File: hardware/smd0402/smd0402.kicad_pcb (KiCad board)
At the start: 2 copper layers, 140 x 40 mm, 79 parts, among them J1 Conn_01x04, J2 Conn_01x03, T1 TestPoint_THTPad_3.0x3.0mm_Dr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, T12 TestPoint_THTPad_3.0x3.0mm_Dr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, T13 TestPoint_THTPad_3.0x3.0mm_Dr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, T14 TestPoint_THTPad_3.0x3.0mm_Dr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, T15 TestPoint_THTPad_3.0x3.0mm_Dr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, T16 TestPoint_THTPad_3.0x3.0mm_Dr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, T18 TestPoint_THTPad_3.0x3.0mm_Dr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, T19 TestPoint_THTPad_3.0x3.0mm_Dr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, T20 TestPoint_THTPad_3.0x3.0mm_Dr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, T21 TestPoint_THTPad_3.0x3.0mm_Dr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, T22 TestPoint_THTPad_3.0x3.0mm_Dr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, T42 TestPoint_THTPad_D1.0mm_Drill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, T43 TestPoint_THTPad_D1.0mm_Drill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, T44 TestPoint_THTPad_D1.0mm_Drill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, T45 TestPoint_THTPad_D1.0mm_Drill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, T46 TestPoint_THTPad_D1.0mm_Drill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, T48 TestPoint_THTPad_D1.0mm_Drill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, T49 TestPoint_THTPad_D1.0mm_Drill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, T50 TestPoint_THTPad_D1.0mm_Drill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, T51 TestPoint_THTPad_D1.0mm_Drill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, T51 TestPoint_THTPad_D2.0mm_Drill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, T52 TestPoint_THTPad_D1.0mm_Drill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, T52 TestPoint_THTPad_D2.0mm_Drill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, T53 TestPoint_THTPad_D2.0mm_Drill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, T54 TestPoint_THTPad_D2.0mm_Drill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, T55 TestPoint_THTPad_D2.0mm_Drill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, T56 TestPoint_THTPad_D2.0mm_Drill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, U1 WCH CH32V003F4U6

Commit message: add repo URL QR on back, tweak text on front
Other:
- board text added: "-"
- board text added: "DC615"
- board text added: "github.com/eutectic6337/coin1"
- board text added: "limited edition"
- board text removed: "LIMITED EDITION"

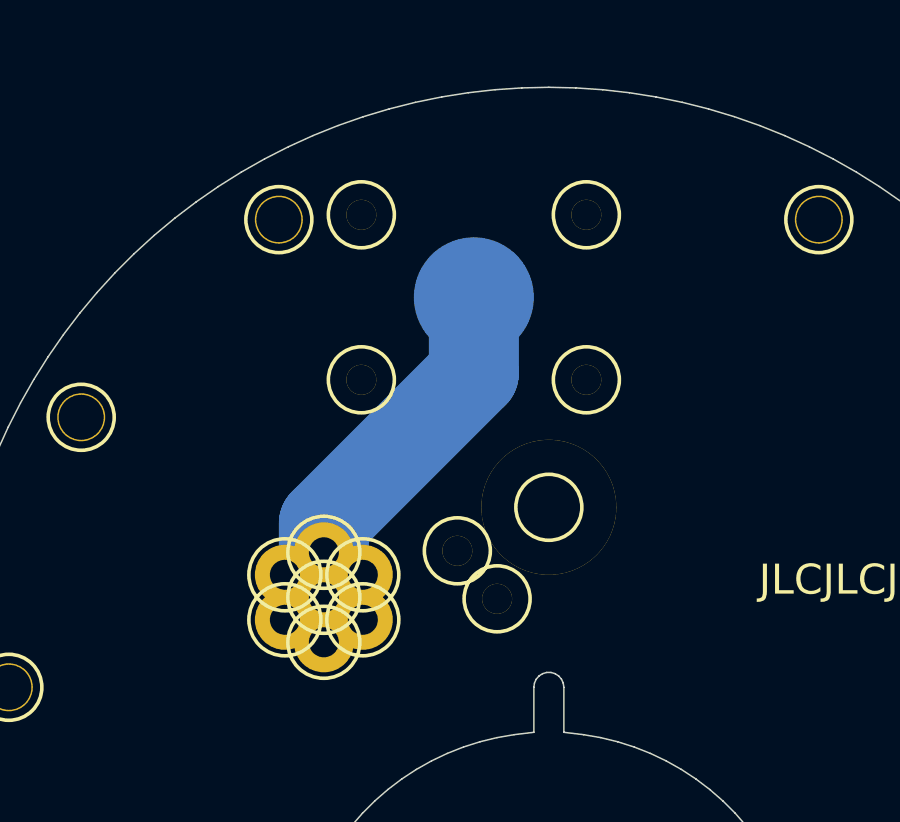
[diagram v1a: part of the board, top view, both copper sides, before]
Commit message: moved clearance holes to match decoupling caps
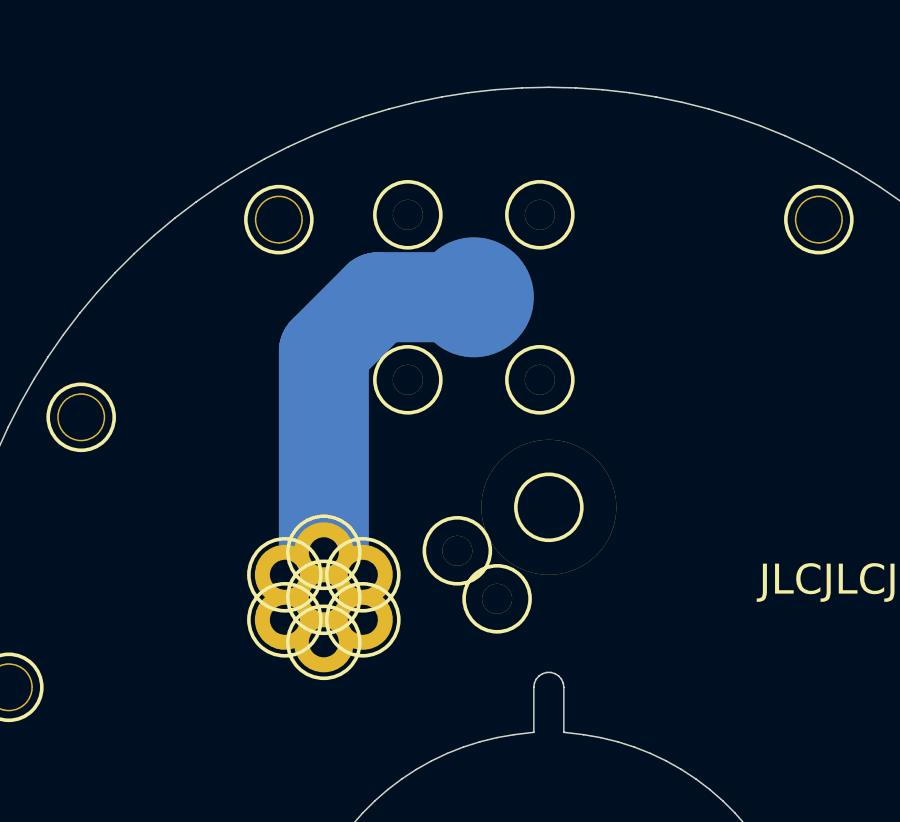
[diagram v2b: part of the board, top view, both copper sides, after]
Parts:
- moved T21 1.55 mm to (95.3, 34.2)
- moved T21 1.55 mm to (99.7, 39.8)
- moved T21 1.55 mm to (95.3, 39.8)
- moved T21 1.55 mm to (99.7, 34.2)
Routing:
- net +3V0: track 58.2 -> 60.1 mm
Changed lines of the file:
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@@
 	(footprint "TestPoint:TestPoint_THTPad_3.0x3.0mm_Drill1.5mm"
 		(layer "F.Cu")
-		(at 93.75 34.25 120)
+		(at 95.3 34.25 120)
 		(descr "THT rectangular pad as test Point, square 3.0mm side length, hole diameter 1.5mm")
 		(tags "test point THT pad rectangle square")
@@
 	(footprint "TestPoint:TestPoint_THTPad_3.0x3.0mm_Drill1.5mm"
 		(layer "F.Cu")
-		(at 101.25 39.75 120)
+		(at 99.7 39.75 120)
 		(descr "THT rectangular pad as test Point, square 3.0mm side length, hole diameter 1.5mm")
 		(tags "test point THT pad rectangle square")
@@
 	(footprint "TestPoint:TestPoint_THTPad_3.0x3.0mm_Drill1.5mm"
 		(layer "F.Cu")
-		(at 93.75 39.75 120)
+		(at 95.3 39.75 120)
 		(descr "THT rectangular pad as test Point, square 3.0mm side length, hole diameter 1.5mm")
 		(tags "test point THT pad rectangle square")
@@
 	(footprint "TestPoint:TestPoint_THTPad_3.0x3.0mm_Drill1.5mm"
 		(layer "F.Cu")
-		(at 101.25 34.25 120)
+		(at 99.7 34.25 120)
 		(descr "THT rectangular pad as test Point, square 3.0mm side length, hole diameter 1.5mm")
 		(tags "test point THT pad rectangle square")
@@
 	)
 	(segment
-		(start 92.5 47)
-		(end 92.5 44.533)
-		(width 3)
-		(layer "B.Cu")
-		(net 3)
-	)
-	(segment
 		(start 47.5 37)
 		(end 47.498 37.002)
@@
 	)
 	(segment
-		(start 142.5 49.5)
-		(end 150 57)
+		(start 92.5 47)
+		(end 92.5 38.8)
 		(width 3)
 		(layer "B.Cu")
@@
 	)
 	(segment
-		(start 92.5 44.533)
-		(end 97.5 39.533)
+		(start 142.5 49.5)
+		(end 150 57)
 		(width 3)
 		(layer "B.Cu")
@@
 	)
 	(segment
+		(start 92.5 38.8)
+		(end 94.3 37)
+		(width 3)
+		(layer "B.Cu")
+		(net 3)
+	)
+	(segment
 		(start 142.5 47)
 		(end 142.5 49.5)
@@
 	)
 	(segment
-		(start 48.3 46.1)
-		(end 48.3 45.5)
-		(width 0.8)
+		(start 94.3 37)
+		(end 97.5 37)
+		(width 3)
 		(layer "B.Cu")
 		(net 3)
 	)
 	(segment
-		(start 97.5 39.533)
-		(end 97.5 37)
-		(width 3)
+		(start 48.3 46.1)
+		(end 48.3 45.5)
+		(width 0.8)
 		(layer "B.Cu")
 		(net 3)

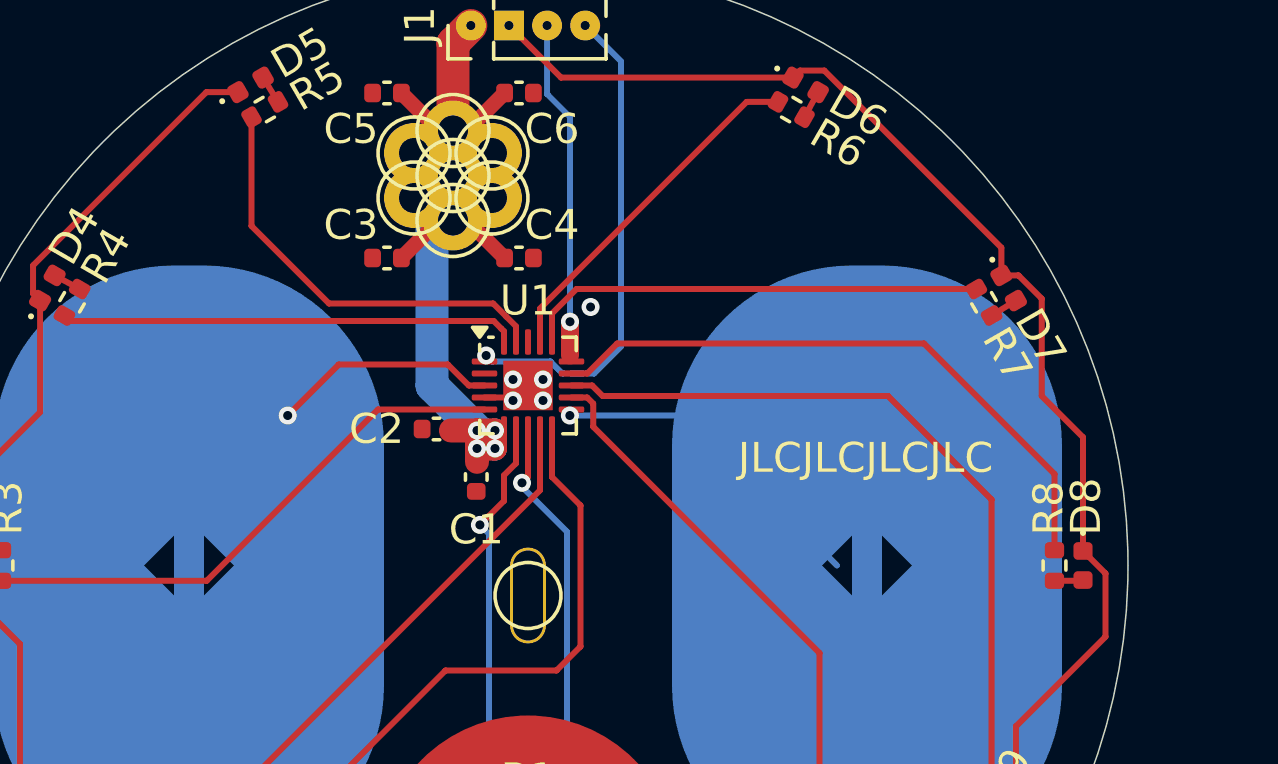
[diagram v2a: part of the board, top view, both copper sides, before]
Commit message: reassign touch pads to OPNx
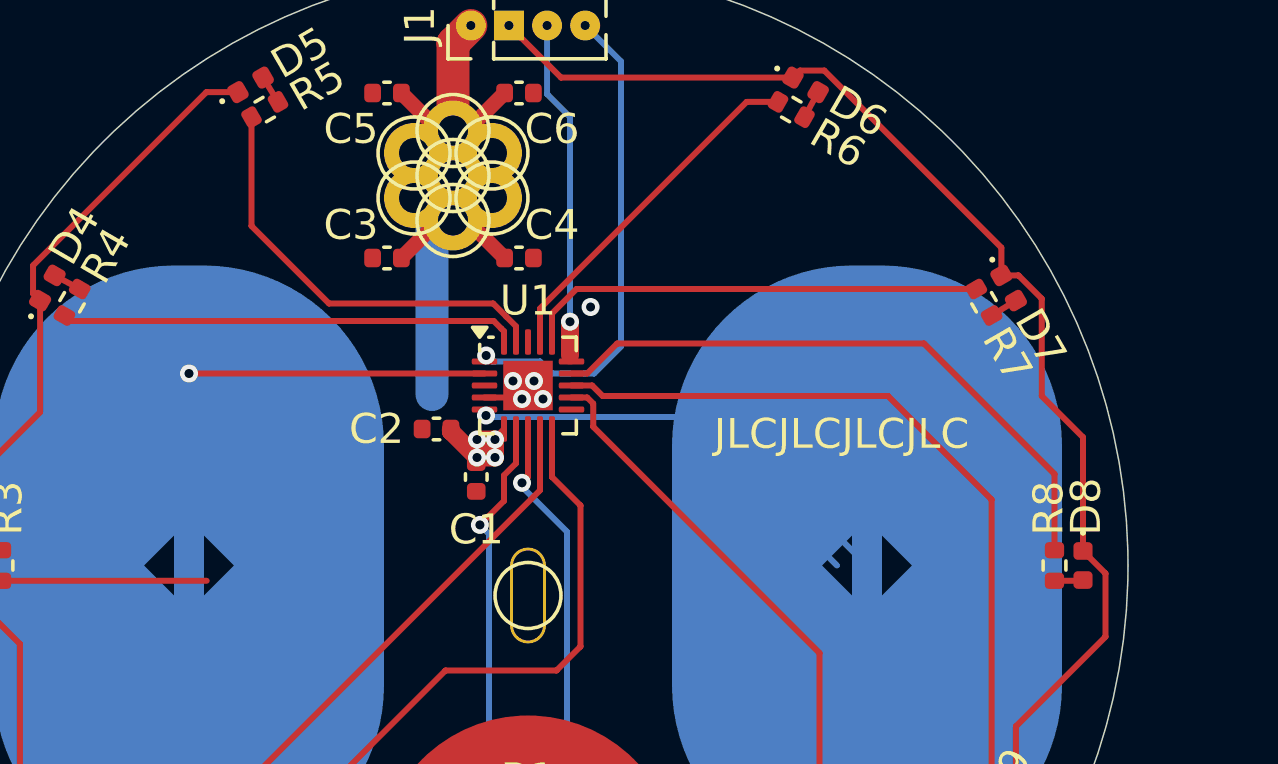
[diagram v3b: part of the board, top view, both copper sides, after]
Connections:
- net /NRST renamed Net-(J1-Pin_4)
- U1 pad 11: /touch2 -> unconnected-(U1-PC4-Pad11)
- U1 pad 2: unconnected-(U1-PA1-Pad2) -> /touch1
- U1 pad 21: GND -> VSS
- U1 pad 3: /touch1 -> unconnected-(U1-PA2-Pad3)
- U1 pad 5: /LED3 -> /touch2
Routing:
- net /LED3: track 18.5 -> 6.84 mm
- net /touch2: track 11.0 -> 21.8 mm
- net +3V0: track 60.1 -> 56.3 mm
- net /touch1: track 7.55 -> 9.85 mm

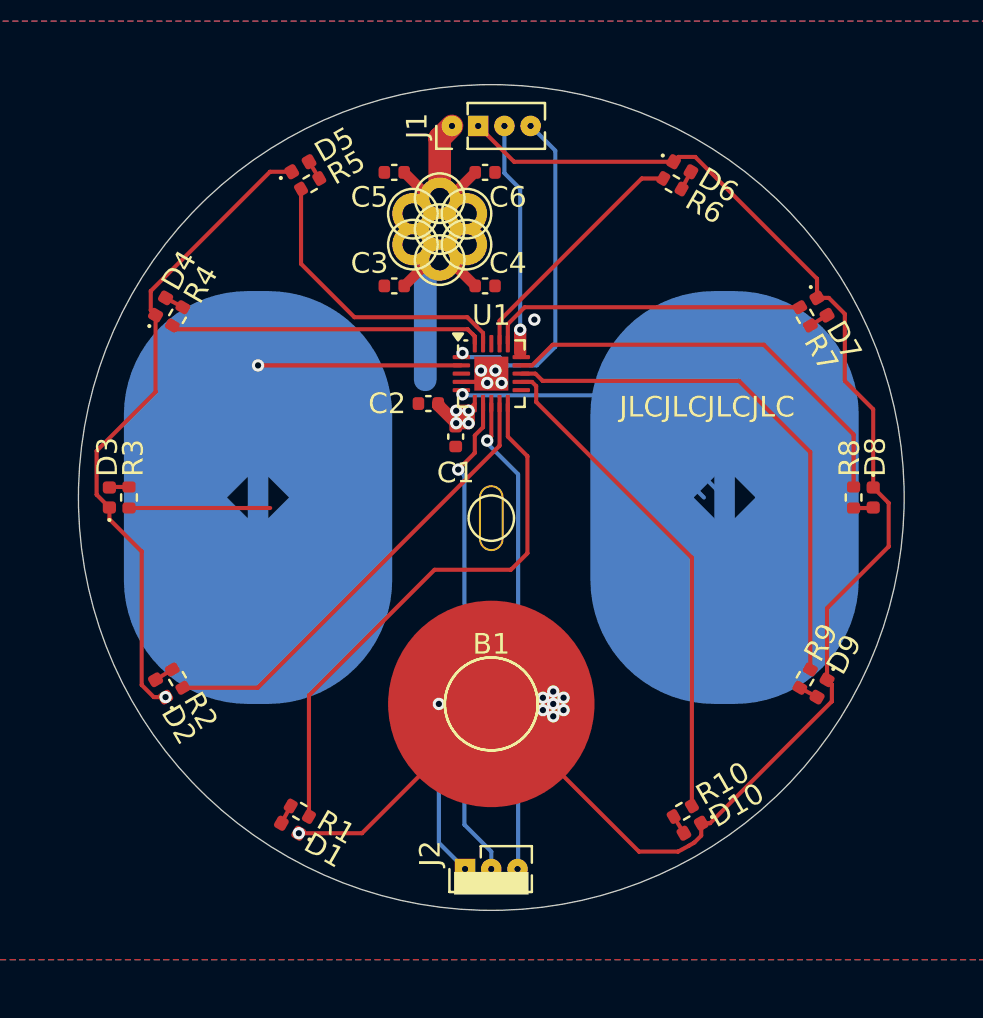
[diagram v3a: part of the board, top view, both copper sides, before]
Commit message: reassign pins for LEDs and touchpads
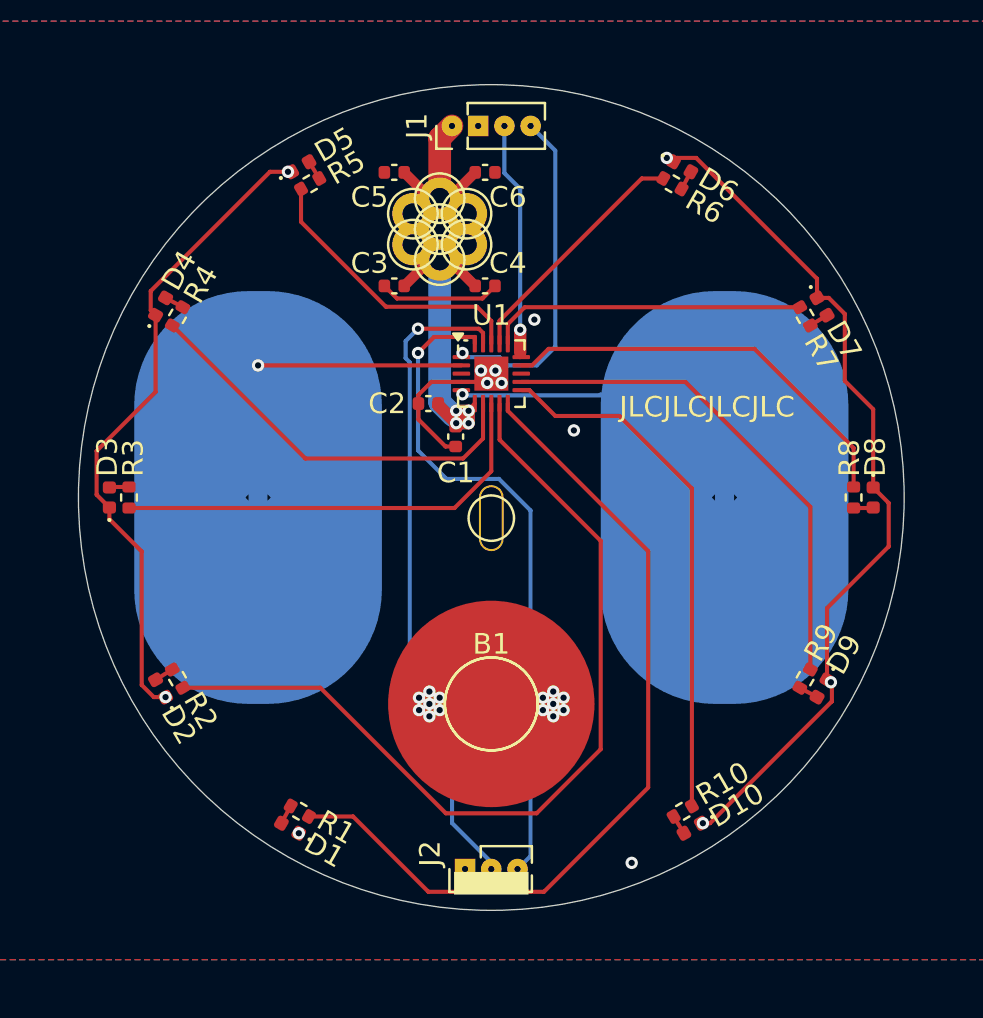
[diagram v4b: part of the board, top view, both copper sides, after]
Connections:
- net Net-(J1-Pin_4) renamed /NRST
- U1 pad 11: unconnected-(U1-PC4-Pad11) -> /LED10
- U1 pad 12: /LED10 -> /LED9
- U1 pad 13: /LED9 -> unconnected-(U1-PC6-Pad13)
- U1 pad 18: unconnected-(U1-PD4-Pad18) -> /LED5
- U1 pad 19: /LED5 -> /TX
- U1 pad 20: /LED4 -> /RX
- U1 pad 7: /TX -> /LED4
- U1 pad 8: /RX -> /LED3
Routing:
- net GND: track 120.2 -> 87.4 mm, vias 15 -> 27
- net /LED2: track 22.2 -> 42.8 mm
- net /LED3: track 6.84 -> 21.6 mm
- net /LED1: track 26.9 -> 41.5 mm
- net /RX: track 23.3 -> 32.8 mm
- net /TX: track 23.7 -> 32.2 mm
- net /LED4: track 15.2 -> 19.8 mm
- net +3V0: track 56.3 -> 59.2 mm
- net /LED9: track 26.1 -> 24.4 mm
- net /LED10: track 24.3 -> 25.6 mm
- net /LED8: track 20.9 -> 20.3 mm

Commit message: change bypass caps from 10n to 1u
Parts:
- C1, C2, C3, C4, C5, C6: value 10n -> 1u
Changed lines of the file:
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@@
 			)
 		)
-		(property "Value" "10n"
+		(property "Value" "1u"
 			(at 0 1.16 0)
 			(layer "F.Fab")
@@
 			)
 		)
-		(property "Datasheet" "https://www.lcsc.com/datasheet/lcsc_datasheet_2304140030_CCTC-TCC0402X7R103M500AT_C696856.pdf"
+		(property "Datasheet" "https://www.lcsc.com/datasheet/lcsc_datasheet_2410121534_CCTC-TCC0402X5R105M160AT_C7393851.pdf"
 			(at 0 0 0)
 			(unlocked yes)
@@
 			)
 		)
-		(property "LCSC" "C696856"
+		(property "LCSC" "C7393851"
 			(at 0 0 0)
 			(unlocked yes)
@@
 			)
 		)
-		(property "Value" "10n"
+		(property "Value" "1u"
 			(at 0 1.16 90)
 			(layer "F.Fab")
@@
 			)
 		)
-		(property "Datasheet" "https://www.lcsc.com/datasheet/lcsc_datasheet_2304140030_CCTC-TCC0402X7R103M500AT_C696856.pdf"
+		(property "Datasheet" "https://www.lcsc.com/datasheet/lcsc_datasheet_2410121534_CCTC-TCC0402X5R105M160AT_C7393851.pdf"
 			(at 0 0 -90)
 			(unlocked yes)
@@
 			)
 		)
-		(property "LCSC" "C696856"
+		(property "LCSC" "C7393851"
 			(at 0 0 -90)
 			(unlocked yes)
@@
 			)
 		)
-		(property "JLC" "0402"
+		(property "JLC" ""
 			(at 0 0 -90)
 			(unlocked yes)
@@
 			)
 		)
-		(property "Value" "10n"
+		(property "Value" "1u"
 			(at 0 1.16 0)
 			(layer "F.Fab")
@@
 			)
 		)
-		(property "Datasheet" "https://www.lcsc.com/datasheet/lcsc_datasheet_2304140030_CCTC-TCC0402X7R103M500AT_C696856.pdf"
+		(property "Datasheet" "https://www.lcsc.com/datasheet/lcsc_datasheet_2410121534_CCTC-TCC0402X5R105M160AT_C7393851.pdf"
 			(at 0 0 180)
 			(unlocked yes)
@@
 			)
 		)
-		(property "LCSC" "C696856"
+		(property "LCSC" "C7393851"
 			(at 0 0 180)
 			(unlocked yes)
@@
 			)
 		)
-		(property "Value" "10n"
+		(property "Value" "1u"
 			(at 0 1.16 0)
 			(layer "F.Fab")
@@
 			)
 		)
-		(property "Datasheet" "https://www.lcsc.com/datasheet/lcsc_datasheet_2304140030_CCTC-TCC0402X7R103M500AT_C696856.pdf"
+		(property "Datasheet" "https://www.lcsc.com/datasheet/lcsc_datasheet_2410121534_CCTC-TCC0402X5R105M160AT_C7393851.pdf"
 			(at 0 0 0)
 			(unlocked yes)
@@
 			)
 		)
-		(property "LCSC" "C696856"
+		(property "LCSC" "C7393851"
 			(at 0 0 0)
 			(unlocked yes)
@@
 			)
 		)
-		(property "Value" "10n"
+		(property "Value" "1u"
 			(at 0 1.16 0)
 			(layer "F.Fab")
@@
 			)
 		)
-		(property "Datasheet" "https://www.lcsc.com/datasheet/lcsc_datasheet_2304140030_CCTC-TCC0402X7R103M500AT_C696856.pdf"
+		(property "Datasheet" "https://www.lcsc.com/datasheet/lcsc_datasheet_2410121534_CCTC-TCC0402X5R105M160AT_C7393851.pdf"
 			(at 0 0 180)
 			(unlocked yes)
@@
 			)
 		)
-		(property "LCSC" "C696856"
+		(property "LCSC" "C7393851"
 			(at 0 0 180)
 			(unlocked yes)
@@
 			)
 		)
-		(property "Value" "10n"
+		(property "Value" "1u"
 			(at 0 1.16 0)
 			(layer "F.Fab")
@@
 			)
 		)
-		(property "Datasheet" "https://www.lcsc.com/datasheet/lcsc_datasheet_2304140030_CCTC-TCC0402X7R103M500AT_C696856.pdf"
+		(property "Datasheet" "https://www.lcsc.com/datasheet/lcsc_datasheet_2410121534_CCTC-TCC0402X5R105M160AT_C7393851.pdf"
 			(at 0 0 180)
 			(unlocked yes)
@@
 			)
 		)
-		(property "LCSC" "C696856"
+		(property "LCSC" "C7393851"
 			(at 0 0 180)
 			(unlocked yes)
